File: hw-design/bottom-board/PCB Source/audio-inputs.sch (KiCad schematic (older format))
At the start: 69 parts, among them J7 NYS215, J8 NYS215, Q10 J110, Q11 J110, Q12 2N7002, Q13 2N7002, Q14 J110, Q15 J110, Q16 2N7002, Q9 2N7002, U8 LM4562

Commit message: change bias voltages to 5V, isolate input GND connections
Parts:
- removed C9: 10uF 16V, Capacitor_SMD:C_0805_2012Metric, symbol bottom-board-rescue:C_Small-Device
- removed RA39, RA40: 10K 1%, Resistor_SMD:R_0603_1608Metric, symbol bottom-board-rescue:R_Small-Device
- added C6: 47uF, Capacitor_SMD:CP_Elec_5x5.4, symbol bottom-board-rescue:CP_Small-Device
- added RA37: 100R 1%, Resistor_SMD:R_0603_1608Metric, symbol bottom-board-rescue:R_Small-Device
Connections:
- net labels added: +5VA, GNDS
- wire segments 198 -> 197
- no-connect marks 0 -> 2
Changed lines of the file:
@@
 Text Notes 2575 7400 0    60   ~ 0
 Op Amp Bypass\ncapacitors
-$Comp
-L bottom-board-rescue:AudioJack3_Switch-Connector J8
-U 1 1 5B52CBDF
-P 4700 5425
-F 0 "J8" H 4700 5875 50  0000 C CNN
-F 1 "NYS215" H 4700 5775 50  0000 C CNN
-F 2 "footprints:NMJ6HCD2" H 4700 5425 50  0001 C CNN
-F 3 "" H 4700 5425 50  0001 C CNN
-F 4 "NYS215" H 4700 5425 60  0001 C CNN "MPN"
-	1    4700 5425
-	1    0    0    -1
-$EndComp
 Text GLabel 4900 6900 2    50   Input ~ 0
 IN1
@@
 Wire Wire Line
 	4900 6900 4800 6900
-Wire Wire Line
-	4800 6500 4850 6500
-Wire Wire Line
-	4850 6500 4850 6700
-Wire Wire Line
-	4900 5225 4950 5225
-Wire Wire Line
-	4950 5225 4950 5425
 Wire Wire Line
 	4900 5625 5000 5625
@@
 	2250 3625 2250 3725
 Connection ~ 2250 3725
-$Comp
-L bottom-board-rescue:R_Small-Device RA?
-U 1 1 5BBE6B93
-P 1250 6475
-AR Path="/54F7244B/5BBE6B93" Ref="RA?"  Part="1"
-AR Path="/54F72C8D/5BBE6B93" Ref="RA39"  Part="1"
-F 0 "RA39" V 1175 6475 50  0000 C CNN
-F 1 "10K 1%" V 1325 6475 50  0000 C CNN
-F 2 "Resistor_SMD:R_0603_1608Metric" H 1250 6475 50  0001 C CNN
-F 3 "" H 1250 6475 50  0001 C CNN
-F 4 "RR0816P-103-D" V 1250 6475 60  0001 C CNN "MPN"
-	1    1250 6475
-	1    0    0    -1
-$EndComp
-$Comp
-L bottom-board-rescue:R_Small-Device RA?
-U 1 1 5BBE6ED1
-P 1250 6825
-AR Path="/54F7244B/5BBE6ED1" Ref="RA?"  Part="1"
-AR Path="/54F72C8D/5BBE6ED1" Ref="RA40"  Part="1"
-F 0 "RA40" V 1175 6825 50  0000 C CNN
-F 1 "10K 1%" V 1325 6825 50  0000 C CNN
-F 2 "Resistor_SMD:R_0603_1608Metric" H 1250 6825 50  0001 C CNN
-F 3 "" H 1250 6825 50  0001 C CNN
-F 4 "RR0816P-103-D" V 1250 6825 60  0001 C CNN "MPN"
-	1    1250 6825
-	1    0    0    -1
-$EndComp
-Wire Wire Line
-	1250 6575 1250 6650
-$Comp
-L bottom-board-rescue:GNDA-power #PWR?
-U 1 1 5BBEFBFA
-P 1250 7075
-AR Path="/54F72B97/5BBEFBFA" Ref="#PWR?"  Part="1"
-AR Path="/54F72C8D/5BBEFBFA" Ref="#PWR031"  Part="1"
-F 0 "#PWR031" H 1250 6825 50  0001 C CNN
-F 1 "GNDA" H 1250 6925 50  0000 C CNN
-F 2 "" H 1250 7075 60  0000 C CNN
-F 3 "" H 1250 7075 60  0000 C CNN
-	1    1250 7075
-	1    0    0    -1
-$EndComp
-Wire Wire Line
-	1250 6925 1250 7000
-Wire Wire Line
-	1475 6925 1475 7000
-Wire Wire Line
-	1475 7000 1250 7000
-Connection ~ 1250 7000
-Wire Wire Line
-	1250 7000 1250 7075
 Wire Wire Line
 	1475 6725 1475 6650
-Wire Wire Line
-	1475 6650 1250 6650
-Connection ~ 1250 6650
-Wire Wire Line
-	1250 6650 1250 6725
-$Comp
-L bottom-board-rescue:+12VA-power #PWR?
-U 1 1 5BC01362
-P 1250 6300
-AR Path="/54F7244B/5BC01362" Ref="#PWR?"  Part="1"
-AR Path="/54F72C8D/5BC01362" Ref="#PWR028"  Part="1"
-F 0 "#PWR028" H 1250 6150 50  0001 C CNN
-F 1 "+12VA" H 1250 6440 50  0000 C CNN
-F 2 "" H 1250 6300 60  0000 C CNN
-F 3 "" H 1250 6300 60  0000 C CNN
-	1    1250 6300
-	1    0    0    -1
-$EndComp
-Wire Wire Line
-	1250 6300 1250 6375
 Text Label 1400 6650 0    39   ~ 0
 INPUT_BIAS
@@
 $Comp
 L bottom-board-rescue:C_Small-Device C?
-U 1 1 5BD34D79
-P 1475 6825
-AR Path="/54F7244B/5BD34D79" Ref="C?"  Part="1"
-AR Path="/54F72C8D/5BD34D79" Ref="C9"  Part="1"
-F 0 "C9" V 1300 6825 50  0000 C CNN
-F 1 "10uF 16V" V 1375 6825 50  0000 C CNN
-F 2 "Capacitor_SMD:C_0805_2012Metric" H 1475 6825 60  0001 C CNN
-F 3 "" H 1475 6825 60  0000 C CNN
-F 4 "CL21A106KOFNNNE" H -3825 1475 50  0001 C CNN "MPN"
-	1    1475 6825
-	-1   0    0    -1
-$EndComp
-$Comp
-L bottom-board-rescue:C_Small-Device C?
 U 1 1 5BD40943
 P 2875 6725
@@
 	0    -1   1    0
 $EndComp
-Wire Wire Line
-	1175 6650 1250 6650
 $Comp
 L bottom-board-rescue:R_Small-Device R?
@@
 $EndComp
 Wire Wire Line
-	4900 5425 4950 5425
-Connection ~ 4950 5425
-Wire Wire Line
-	4950 5425 4950 5525
-Wire Wire Line
-	4900 5525 4950 5525
-Connection ~ 4950 5525
-Wire Wire Line
-	4950 5525 4950 5725
-Wire Wire Line
 	4900 5725 4950 5725
-Connection ~ 4950 5725
 Wire Wire Line
 	4950 5725 4950 5875
 Wire Wire Line
 	4800 7000 4850 7000
-Connection ~ 4850 7000
 Wire Wire Line
 	4850 7000 4850 7150
-Wire Wire Line
-	4800 6800 4850 6800
-Connection ~ 4850 6800
-Wire Wire Line
-	4850 6800 4850 7000
-Wire Wire Line
-	4800 6700 4850 6700
-Connection ~ 4850 6700
-Wire Wire Line
-	4850 6700 4850 6800
 Text Notes 8205 4925 0    60   ~ 0
 GPIO controllable gain spec:
+Wire Wire Line
+	1175 6650 1297 6650
+Wire Wire Line
+	1475 6925 1475 6999
+$Comp
+L bottom-board-rescue:GNDA-power #PWR?
+U 1 1 5BBEFBFA
+P 1475 6999
+AR Path="/54F72B97/5BBEFBFA" Ref="#PWR?"  Part="1"
+AR Path="/54F72C8D/5BBEFBFA" Ref="#PWR031"  Part="1"
+F 0 "#PWR031" H 1475 6749 50  0001 C CNN
+F 1 "GNDA" H 1475 6849 50  0000 C CNN
+F 2 "" H 1475 6999 60  0000 C CNN
+F 3 "" H 1475 6999 60  0000 C CNN
+	1    1475 6999
+	1    0    0    -1
+$EndComp
+Connection ~ 1475 6999
+Wire Wire Line
+	1475 6999 1475 7000
+$Comp
+L bottom-board-rescue:CP_Small-Device C?
+U 1 1 5FD12E58
+P 1475 6825
+AR Path="/54F72B97/5FD12E58" Ref="C?"  Part="1"
+AR Path="/54F72C8D/5FD12E58" Ref="C6"  Part="1"
+F 0 "C6" H 1523 6726 50  0000 L CNN
+F 1 "47uF" H 1253 6737 50  0000 L CNN
+F 2 "Capacitor_SMD:CP_Elec_5x5.4" H 1475 6825 60  0001 C CNN
+F 3 "" H 1475 6825 60  0000 C CNN
+F 4 "EDK476M016A9DAA" H -3875 5175 50  0001 C CNN "MPN"
+	1    1475 6825
+	1    0    0    -1
+$EndComp
+$Comp
+L bottom-board-rescue:+5VA-power #PWR?
+U 1 1 5FD12E5E
+P 1297 6337
+AR Path="/54F72B97/5FD12E5E" Ref="#PWR?"  Part="1"
+AR Path="/54F72C8D/5FD12E5E" Ref="#PWR0103"  Part="1"
+F 0 "#PWR0103" H 1297 6187 50  0001 C CNN
+F 1 "+5VA" H 1297 6477 50  0000 C CNN
+F 2 "" H 1297 6337 60  0000 C CNN
+F 3 "" H 1297 6337 60  0000 C CNN
+	1    1297 6337
+	-1   0    0    -1
+$EndComp
+Connection ~ 1297 6650
+Wire Wire Line
+	1297 6650 1475 6650
+Wire Wire Line
+	1297 6590 1297 6591
+Wire Wire Line
+	1297 6337 1297 6391
+$Comp
+L bottom-board-rescue:R_Small-Device RA37
+U 1 1 5FCF26B2
+P 1297 6491
+F 0 "RA37" H 1347 6466 50  0000 L CNN
+F 1 "100R 1%" H 1347 6541 50  0000 L CNN
+F 2 "Resistor_SMD:R_0603_1608Metric" H 1297 6491 60  0001 C CNN
+F 3 "" H 1297 6491 60  0000 C CNN
+F 4 "RR0816P-101-D" H -3353 4991 50  0001 C CNN "MPN"
+	1    1297 6491
+	1    0    0    -1
+$EndComp
+Connection ~ 1297 6391
+Wire Wire Line
+	1297 6391 1297 6392
+Connection ~ 1297 6591
+Wire Wire Line
+	1297 6591 1297 6650
+$Comp
+L bottom-board-rescue:AudioJack3_Switch-Connector J8
+U 1 1 5B52CBDF
+P 4700 5425
+F 0 "J8" H 4700 5875 50  0000 C CNN
+F 1 "NYS215" H 4700 5775 50  0000 C CNN
+F 2 "footprints:NMJ6HCD2" H 4700 5425 50  0001 C CNN
+F 3 "" H 4700 5425 50  0001 C CNN
+F 4 "NYS215" H 4700 5425 60  0001 C CNN "MPN"
+	1    4700 5425
+	1    0    0    -1
+$EndComp
+$Comp
+L power:GNDS #PWR0173
+U 1 1 5FE0AF18
+P 4861 4924
+F 0 "#PWR0173" H 4861 4674 50  0001 C CNN
+F 1 "GNDS" H 4866 4751 50  0000 C CNN
+F 2 "" H 4861 4924 50  0001 C CNN
+F 3 "" H 4861 4924 50  0001 C CNN
+	1    4861 4924
+	-1   0    0    1
+$EndComp
+Wire Wire Line
+	4900 5425 4955 5425
+Wire Wire Line
+	4955 4968 4861 4968
+Wire Wire Line
+	4861 4968 4861 4924
+Wire Wire Line
+	4955 5425 4955 5225
+Wire Wire Line
+	4900 5225 4955 5225
+Connection ~ 4955 5225
+Wire Wire Line
+	4955 5225 4955 4968
+$Comp
+L power:GNDS #PWR0206
+U 1 1 5FE3ABB7
+P 4734 6263
+F 0 "#PWR0206" H 4734 6013 50  0001 C CNN
+F 1 "GNDS" H 4739 6090 50  0000 C CNN
+F 2 "" H 4734 6263 50  0001 C CNN
+F 3 "" H 4734 6263 50  0001 C CNN
+	1    4734 6263
+	-1   0    0    1
+$EndComp
+Wire Wire Line
+	4800 6700 4834 6700
+Wire Wire Line
+	4834 6700 4834 6500
+Wire Wire Line
+	4834 6286 4734 6286
+Wire Wire Line
+	4734 6286 4734 6263
+Wire Wire Line
+	4800 6500 4834 6500
+Connection ~ 4834 6500
+Wire Wire Line
+	4834 6500 4834 6286
+NoConn ~ 4900 5525
+NoConn ~ 4800 6800
 $EndSCHEMATC

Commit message: redo input circuitery
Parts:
- removed R85: 10K, Resistor_SMD:R_0603_1608Metric, symbol bottom-board-rescue:R_Small-Device
- removed RA37: 100R 1%, Resistor_SMD:R_0603_1608Metric, symbol bottom-board-rescue:R_Small-Device
- added C? (x8): 100nF, Capacitor_SMD:C_0603_1608Metric, symbol bottom-board-rescue:C_Small-Device
- added R? (x5): 1K, Resistor_SMD:R_0603_1608Metric, symbol bottom-board-rescue:R_Small-Device
- added R? (x2): 56K, Resistor_SMD:R_0603_1608Metric, symbol bottom-board-rescue:R_Small-Device
- added R?: 100K, Resistor_SMD:R_0603_1608Metric, symbol bottom-board-rescue:R_Small-Device
- added R?: 1K5, Resistor_SMD:R_0603_1608Metric, symbol bottom-board-rescue:R_Small-Device
- Q10, Q11: MPN PMBFJ110,215 -> MMBFJ110
- R18: MPN RT0603BRD071ML -> (none)
- R84: value 10K -> 100K; MPN RR0816P-103-D -> (none)
- RA3: value 5K62 1% -> 5K6 1%; MPN ERA-3AEB5621V -> (none)
- RA4: value 21K 1% -> 22K 1%; MPN RR0816P-2102-D-32C -> (none)
- RA5, RA6: value 4K99 1% -> 4K7 1%; MPN ERA-3AEB4991V -> (none)
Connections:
- net labels added: +10V
- net labels removed: GNDS, IN1, IN2
- wire segments 197 -> 226
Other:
- moved on the sheet: C10, C37, C6, CA10, CA3, CA4, CA5, CA6, CA7, CA8, CA9, D16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

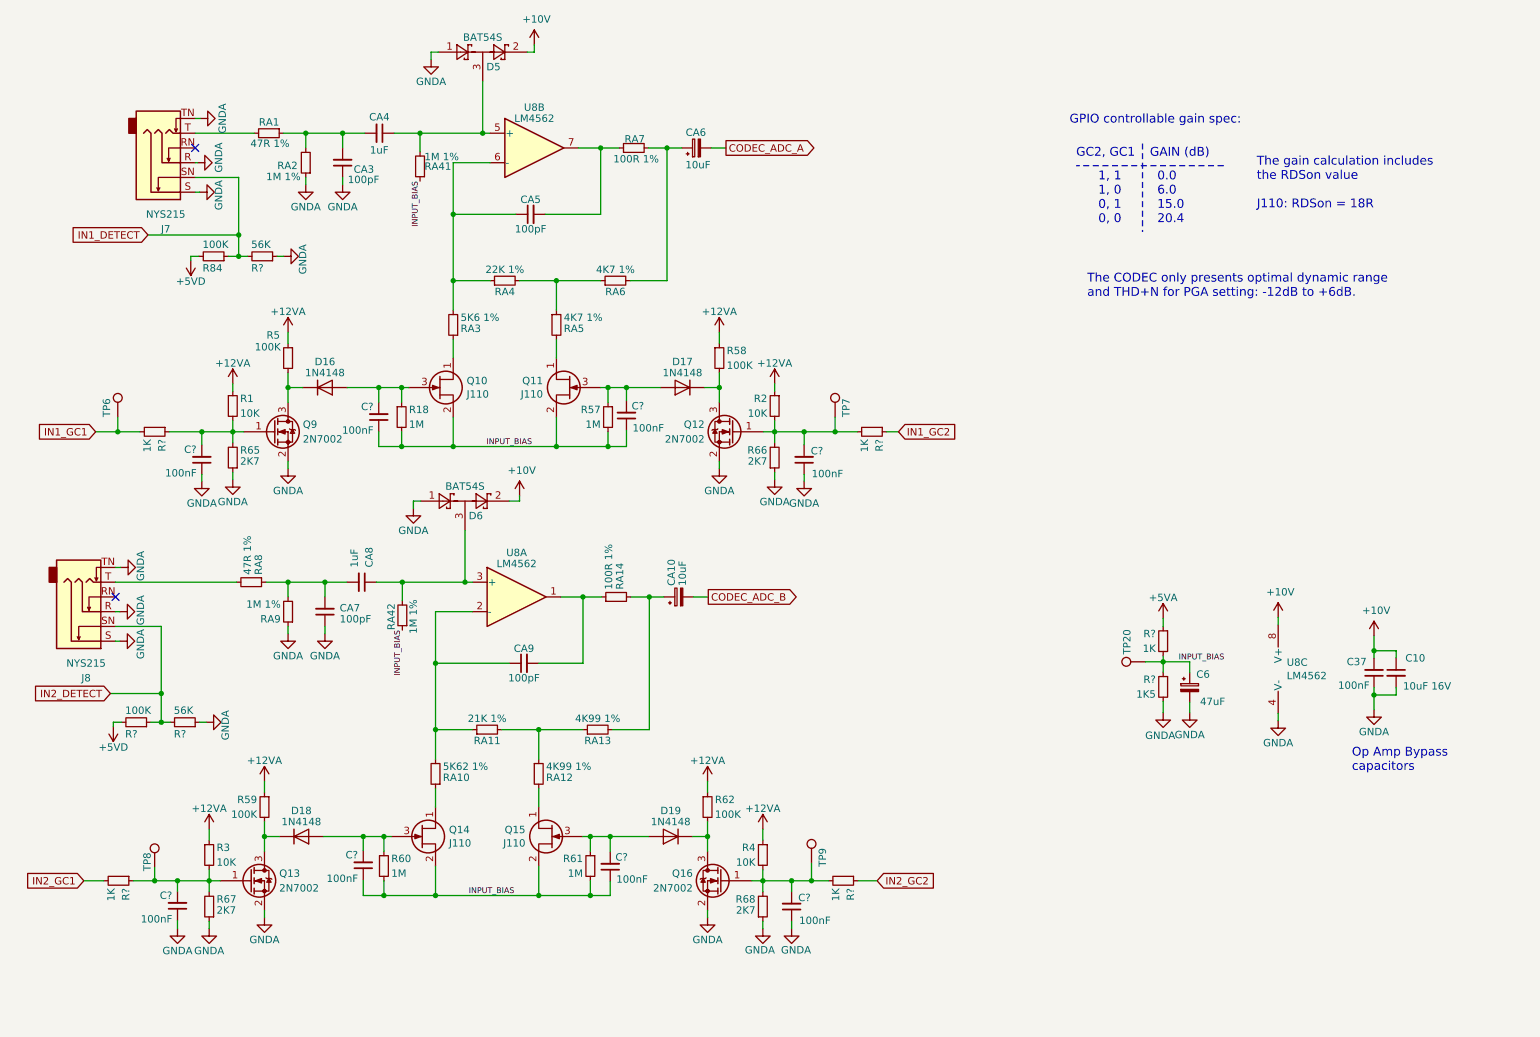
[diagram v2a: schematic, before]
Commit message: place new power curcuit on the PCB
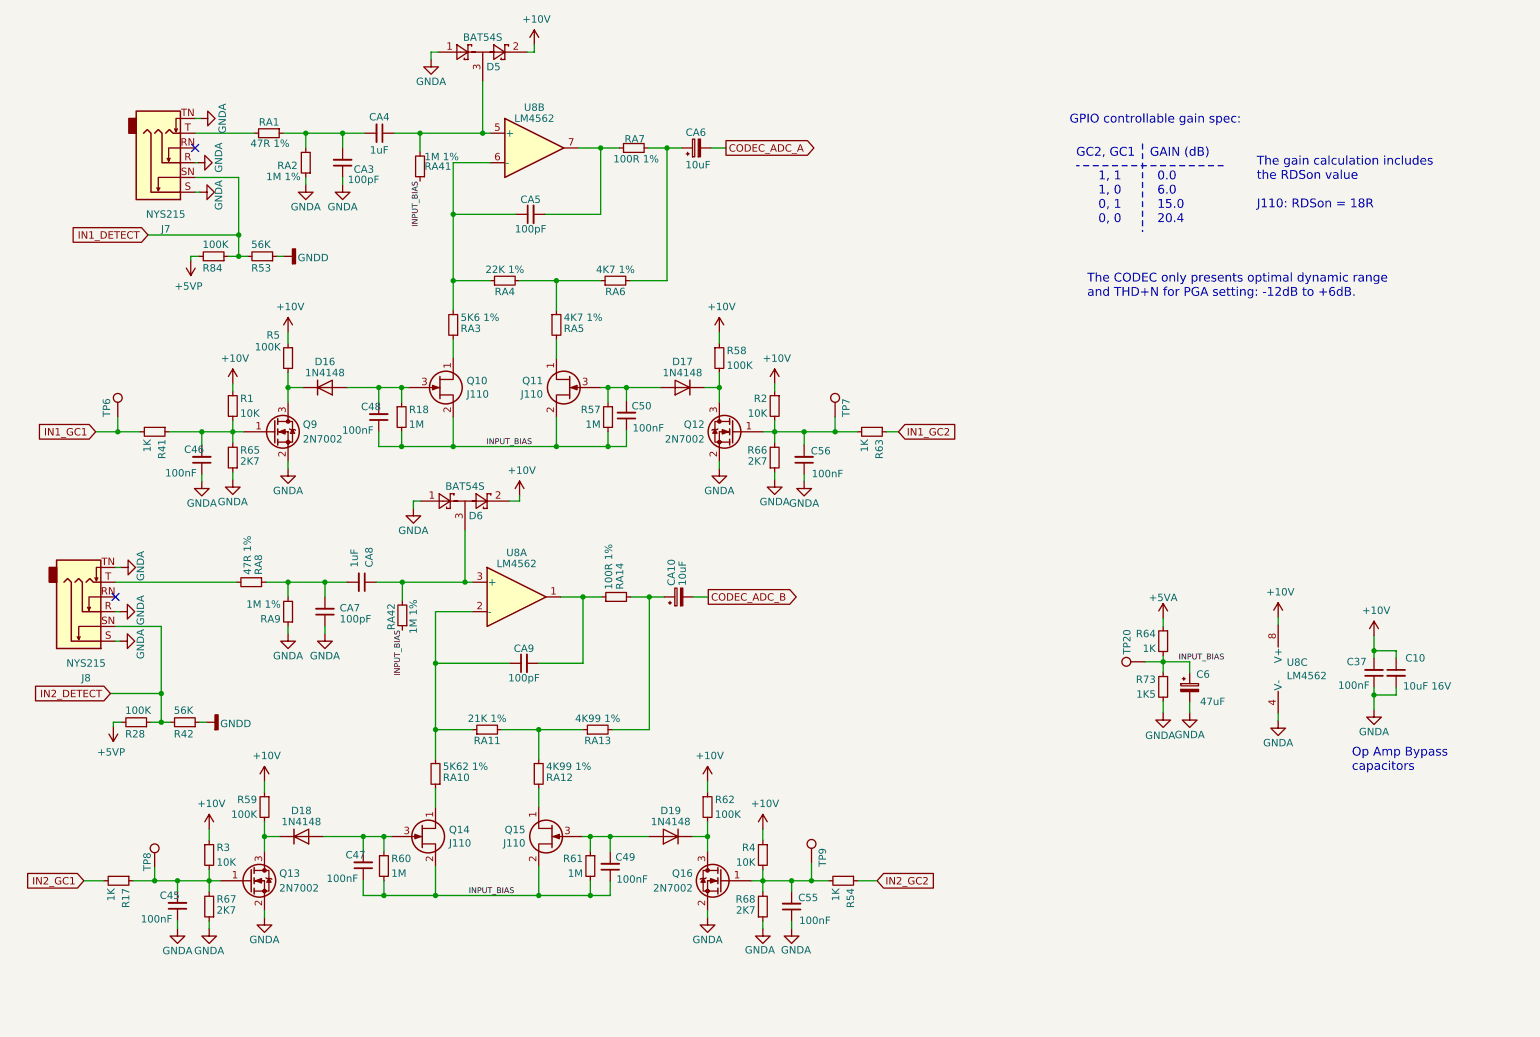
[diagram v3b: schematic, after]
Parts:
- Q14, Q15: MPN PMBFJ110,215 -> MMBFJ110
- gave numbers to parts that had none: 17
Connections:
- net +12VA is gone; now on net +10V: R1.1, R2.1, R3.1, R4.1, R5.1, R58.1, R59.1, R62.1
- net GNDA: no longer R42.1, R53.1
- net +5VD renamed +5VP
- new net GNDD: R42.1, R53.1

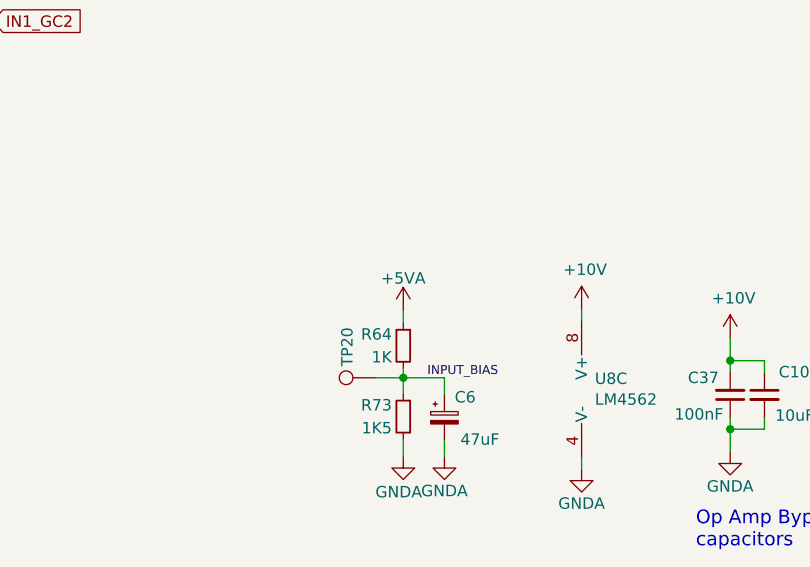
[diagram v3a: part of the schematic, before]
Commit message: use 10V for output detect pins
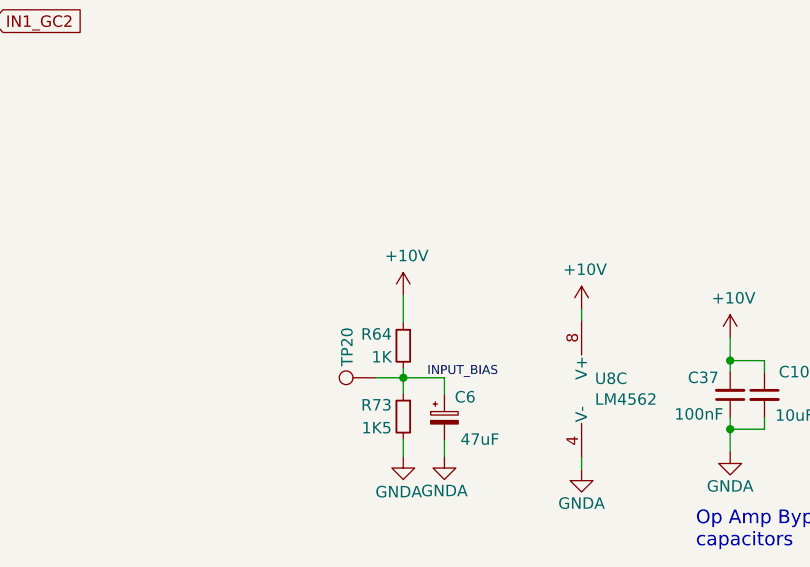
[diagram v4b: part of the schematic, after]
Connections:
- net +5VA is gone; now on net +10V: R64.1
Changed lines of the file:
@@
 Wire Wire Line
 	8660 5295 8660 5220
-$Comp
-L bottom-board-rescue:+5VA-power #PWR?
-U 1 1 5FD12E5E
-P 8660 4655
-AR Path="/54F72B97/5FD12E5E" Ref="#PWR?"  Part="1"
-AR Path="/54F72C8D/5FD12E5E" Ref="#PWR0103"  Part="1"
-F 0 "#PWR0103" H 8660 4505 50  0001 C CNN
-F 1 "+5VA" H 8660 4795 50  0000 C CNN
-F 2 "" H 8660 4655 60  0000 C CNN
-F 3 "" H 8660 4655 60  0000 C CNN
-	1    8660 4655
-	-1   0    0    -1
-$EndComp
 Wire Wire Line
 	8540 4950 8660 4950
@@
 Wire Wire Line
 	8660 4910 8660 4950
-Wire Wire Line
-	8660 4710 8660 4655
 $Comp
 L power:+10V #PWR0274
@@
 $EndComp
 $Comp
-L power:+10V #PWR?
+L power:+10V #PWR0129
 U 1 1 641A4CB0
 P 5945 6085
-F 0 "#PWR?" H 5945 5935 50  0001 C CNN
+F 0 "#PWR0129" H 5945 5935 50  0001 C CNN
 F 1 "+10V" H 5960 6258 50  0000 C CNN
 F 2 "" H 5945 6085 50  0001 C CNN
@@
 $EndComp
 $Comp
-L power:+10V #PWR?
+L power:+10V #PWR0130
 U 1 1 641A6AAF
 P 5570 5760
-F 0 "#PWR?" H 5570 5610 50  0001 C CNN
+F 0 "#PWR0130" H 5570 5610 50  0001 C CNN
 F 1 "+10V" H 5585 5933 50  0000 C CNN
 F 2 "" H 5570 5760 50  0001 C CNN
@@
 $EndComp
 $Comp
-L power:+10V #PWR?
+L power:+10V #PWR0181
 U 1 1 641A7976
 P 2565 5760
-F 0 "#PWR?" H 2565 5610 50  0001 C CNN
+F 0 "#PWR0181" H 2565 5610 50  0001 C CNN
 F 1 "+10V" H 2580 5933 50  0000 C CNN
 F 2 "" H 2565 5760 50  0001 C CNN
@@
 $EndComp
 $Comp
-L power:+10V #PWR?
+L power:+10V #PWR0209
 U 1 1 641AB1CC
 P 2190 6085
-F 0 "#PWR?" H 2190 5935 50  0001 C CNN
+F 0 "#PWR0209" H 2190 5935 50  0001 C CNN
 F 1 "+10V" H 2205 6258 50  0000 C CNN
 F 2 "" H 2190 6085 50  0001 C CNN
@@
 $EndComp
 $Comp
-L power:+10V #PWR?
+L power:+10V #PWR0212
 U 1 1 641AD040
 P 2350 3065
-F 0 "#PWR?" H 2350 2915 50  0001 C CNN
+F 0 "#PWR0212" H 2350 2915 50  0001 C CNN
 F 1 "+10V" H 2365 3238 50  0000 C CNN
 F 2 "" H 2350 3065 50  0001 C CNN
@@
 $EndComp
 $Comp
-L power:+10V #PWR?
+L power:+10V #PWR0333
 U 1 1 641B09C8
 P 2725 2715
-F 0 "#PWR?" H 2725 2565 50  0001 C CNN
+F 0 "#PWR0333" H 2725 2565 50  0001 C CNN
 F 1 "+10V" H 2740 2888 50  0000 C CNN
 F 2 "" H 2725 2715 50  0001 C CNN
@@
 $EndComp
 $Comp
-L power:+10V #PWR?
+L power:+10V #PWR0334
 U 1 1 641B1BD1
 P 5650 2715
-F 0 "#PWR?" H 5650 2565 50  0001 C CNN
+F 0 "#PWR0334" H 5650 2565 50  0001 C CNN
 F 1 "+10V" H 5665 2888 50  0000 C CNN
 F 2 "" H 5650 2715 50  0001 C CNN
@@
 $EndComp
 $Comp
-L power:+10V #PWR?
+L power:+10V #PWR0335
 U 1 1 641B34C6
 P 6025 3065
-F 0 "#PWR?" H 6025 2915 50  0001 C CNN
+F 0 "#PWR0335" H 6025 2915 50  0001 C CNN
 F 1 "+10V" H 6040 3238 50  0000 C CNN
 F 2 "" H 6025 3065 50  0001 C CNN
@@
 	1    0    0    -1
 $EndComp
+$Comp
+L power:+10V #PWR0103
+U 1 1 641FD742
+P 8660 4590
+F 0 "#PWR0103" H 8660 4440 50  0001 C CNN
+F 1 "+10V" H 8675 4763 50  0000 C CNN
+F 2 "" H 8660 4590 50  0001 C CNN
+F 3 "" H 8660 4590 50  0001 C CNN
+	1    8660 4590
+	1    0    0    -1
+$EndComp
+Wire Wire Line
+	8660 4590 8660 4710
 $EndSCHEMATC
